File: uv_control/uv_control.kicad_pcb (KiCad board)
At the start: 2 copper layers, 20 parts, among them J1 Safety, J2 Fan, J3 12V Power, J4 Light Power, Q1 BSS138, Q2 BSS138, Q3 IRFS7730-7, U1 L7805, U2 MCP1415

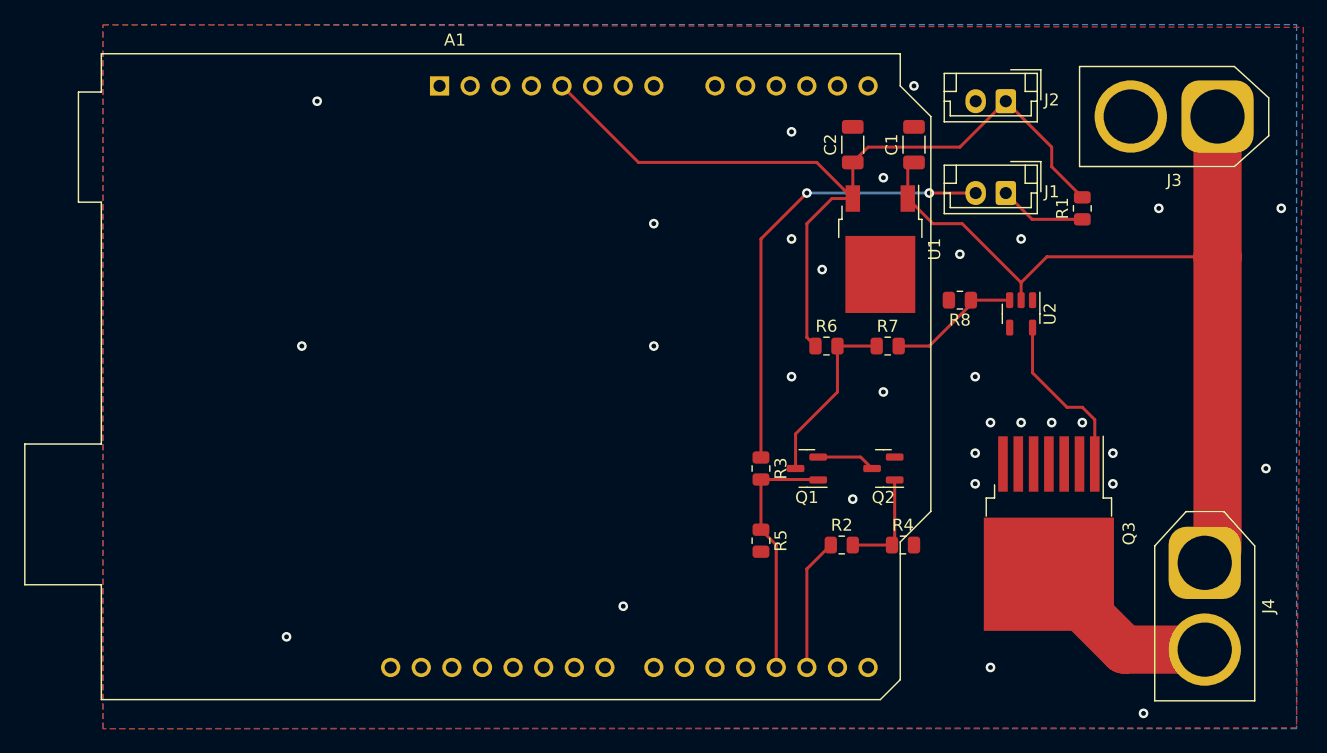
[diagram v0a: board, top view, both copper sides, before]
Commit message: Updating control board to include more pinouts
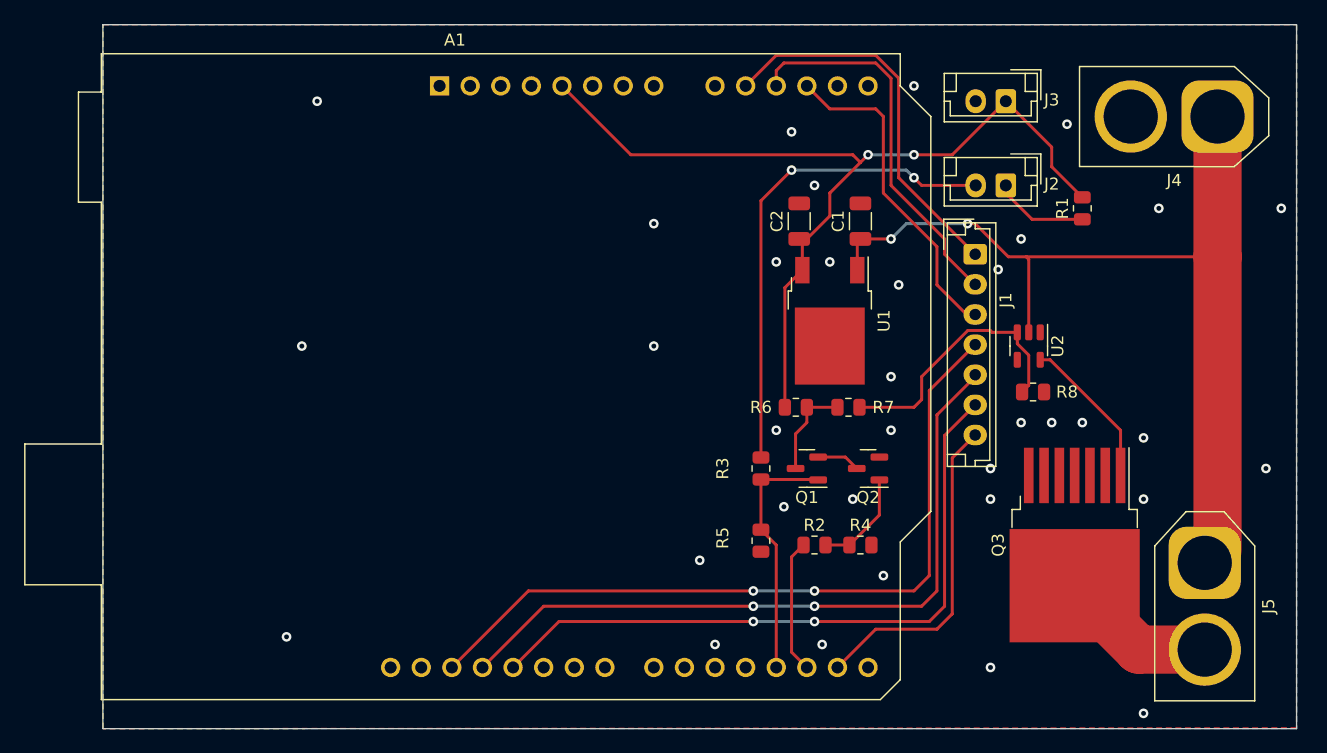
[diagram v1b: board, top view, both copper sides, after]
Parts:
- added J1: Keypad, Connector_JST:JST_EH_B7B-EH-A_1x07_P2.50mm_Vertical, F.Cu at (191.8, 85.1)
- moved R8 9.74 mm to (196.6, 96.5), turned to 0 degrees
- moved C2 7.75 mm to (177.2, 82.3)
- moved C1 7.75 mm to (182.2, 82.3)
- moved U1 7.27 mm to (179.7, 90.6)
- moved R7 6.03 mm to (181.3, 97.8)
- moved R6 5.68 mm to (176.9, 97.8)
- moved R4 3.53 mm to (182.2, 109.2)
- moved U2 2.75 mm to (196.2, 92.7)
- moved Q3 2.34 mm to (200.0, 109.2)
- moved R2 2.26 mm to (178.4, 109.2)
- moved Q2 1.27 mm to (182.9, 102.9)
- moved J2 0.64 mm to (194.3, 79.4)
- renumbered J1 to J2, J2 to J3, J3 to J4, J4 to J5
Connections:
- A1 pad 10: unconnected-(A1-Pad10) -> /Keypad_1
- A1 pad 11: unconnected-(A1-Pad11) -> /Keypad_2
- A1 pad 12: unconnected-(A1-Pad12) -> /Keypad_3
- A1 pad 16: unconnected-(A1-Pad16) -> Net-(A1-Pad16)
- A1 pad 26: unconnected-(A1-Pad26) -> Net-(A1-Pad26)
- A1 pad 27: unconnected-(A1-Pad27) -> Net-(A1-Pad27)
- A1 pad 28: unconnected-(A1-Pad28) -> Net-(A1-Pad28)
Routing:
- net Net-(A1-Pad28): track 0.00 -> 63.5 mm, vias 0 -> 2
- net Net-(A1-Pad27): track 0.00 -> 59.6 mm, vias 0 -> 2
- net Net-(A1-Pad26): track 0.00 -> 55.7 mm, vias 0 -> 2
- net /Keypad_1: track 0.00 -> 31.8 mm
- net /Keypad_2: track 0.00 -> 31.6 mm
- net /Keypad_3: track 0.00 -> 27.4 mm
- net Net-(A1-Pad16): track 0.00 -> 27.0 mm
- net Net-(R7-Pad2): track 11.0 -> 22.5 mm
- net Net-(Q1-Pad3): track 14.9 -> 8.01 mm
- net +12V: track 71.6 -> 77.8 mm, vias 0 -> 2
- net +5V: track 71.5 -> 75.7 mm, vias 0 -> 2
- net Net-(J2-Pad2): track 37.5 -> 40.7 mm
- net Net-(J5-Pad2): track 15.5 -> 13.0 mm
- net Net-(Q3-Pad1): track 14.2 -> 12.8 mm
- net Net-(Q1-Pad2): track 4.87 -> 3.60 mm
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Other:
- board outline added: 99.1 x 58.4 mm

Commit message: Updating PCB to change to 2 layer setup
Added LCD schematic, removing LCD shield design
Fixed XT60 polarity
Added Status LED and Safety LED
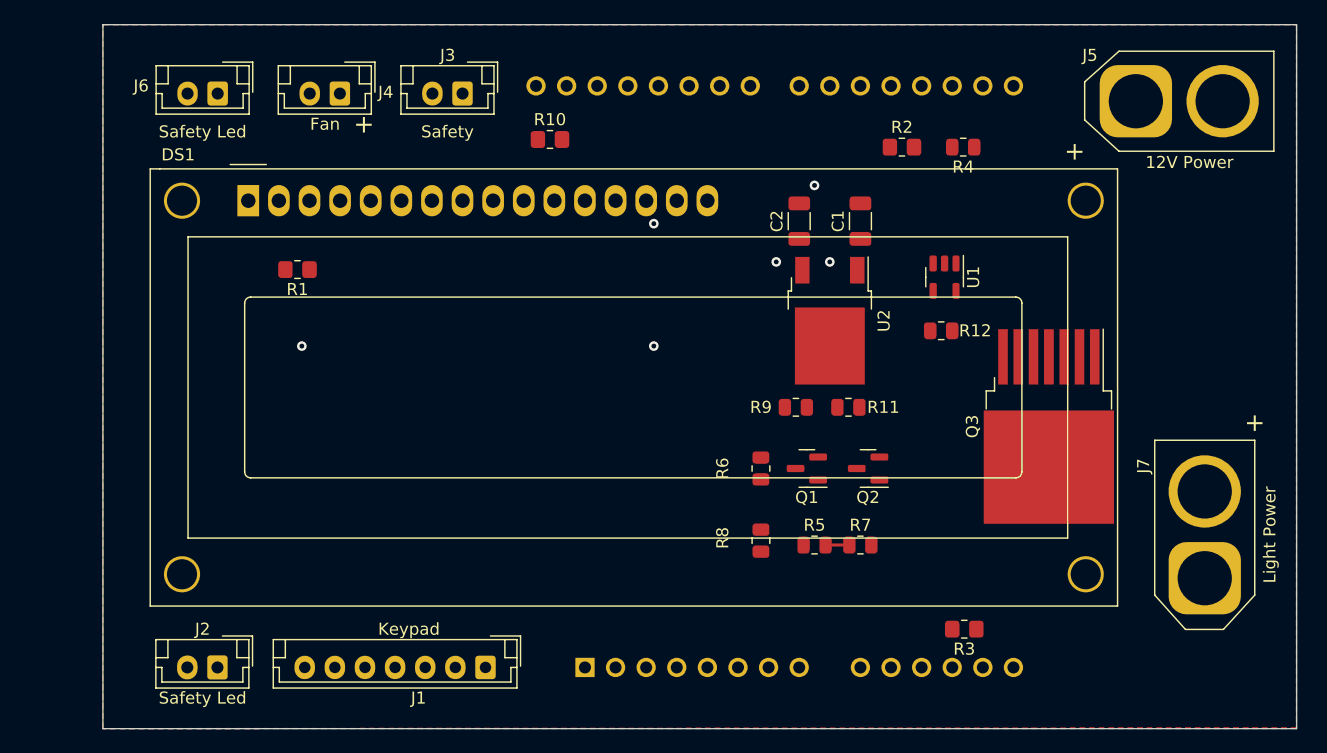
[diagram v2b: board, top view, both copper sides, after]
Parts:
- added DS1: WC1602A, Display:WC1602A, F.Cu at (131.4, 80.6)
- added J2: Safety Led, Connector_JST:JST_EH_B2B-EH-A_1x02_P2.50mm_Vertical, F.Cu at (128.9, 119.4)
- added J6: Safety Led, Connector_JST:JST_EH_B2B-EH-A_1x02_P2.50mm_Vertical, F.Cu at (128.9, 71.8)
- added R1: 10K, Resistor_SMD:R_0805_2012Metric_Pad1.20x1.40mm_HandSolder, F.Cu at (135.5, 86.4)
- added R10: 220, Resistor_SMD:R_0805_2012Metric_Pad1.20x1.40mm_HandSolder, F.Cu at (156.5, 75.6)
- added R2: 220, Resistor_SMD:R_0805_2012Metric_Pad1.20x1.40mm_HandSolder, F.Cu at (185.7, 76.2)
- added R3: 220, Resistor_SMD:R_0805_2012Metric_Pad1.20x1.40mm_HandSolder, F.Cu at (190.9, 116.2)
- A1: moved to B.Cu
- moved J4 55.3 mm to (139.0, 71.8)
- moved J1 53.2 mm to (151.1, 119.4), turned to 180 degrees
- moved A1 49.7 mm to (159.4, 119.4)
- moved J3 45.7 mm to (149.2, 71.8)
- moved R4 11.1 mm to (190.8, 76.2), turned to 180 degrees
- moved Q3 10.1 mm to (197.9, 99.4)
- moved R12 9.16 mm to (189.0, 91.4)
- moved U1 9.03 mm to (189.2, 87.0)
- moved J5 6.89 mm to (205.1, 72.4), turned to 0 degrees
- moved J7 1.27 mm to (210.8, 112.0), turned to 90 degrees
- renumbered J2 to J3, J3 to J4, J4 to J5, J5 to J7, R7 to R11, R8 to R12, R1 to R4, R2 to R5, R3 to R6, R4 to R7, R5 to R8, R6 to R9, U2 to U1, U1 to U2
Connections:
- net Net-(A1-Pad17) renamed /output_en
- A1 pad 13: unconnected-(A1-Pad13) -> /Keypad_4
- A1 pad 14: unconnected-(A1-Pad14) -> /safety_led
- A1 pad 16: Net-(A1-Pad16) -> unconnected-(A1-Pad16)
- A1 pad 19: unconnected-(A1-Pad19) -> /LCD_D4
- A1 pad 20: unconnected-(A1-Pad20) -> /LCD_D5
- A1 pad 21: unconnected-(A1-Pad21) -> /LCD_D6
- A1 pad 22: unconnected-(A1-Pad22) -> /LCD_D7
- A1 pad 23: unconnected-(A1-Pad23) -> /LCD_E
- A1 pad 24: unconnected-(A1-Pad24) -> /LCD_RS
- A1 pad 25: unconnected-(A1-Pad25) -> /status_led1
- J1 pad 7: Net-(A1-Pad16) -> /Keypad_4
- J5 pad 1: +12V -> GND
- J5 pad 2: GND -> +12V
- J7 pad 1: +12V -> Net-(Q3-Pad8)
- J7 pad 2: Net-(J5-Pad2) -> +12V
- Q3 pad 8: Net-(J5-Pad2) -> Net-(Q3-Pad8)
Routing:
- net +12V: track 77.8 -> 0.37 mm, vias 2 -> 0
- net +5V: track 75.7 -> 1.00 mm, vias 2 -> 0
- net Net-(A1-Pad28): track 63.5 -> 0.00 mm, vias 2 -> 0
- net Net-(A1-Pad27): track 59.6 -> 0.00 mm, vias 2 -> 0
- net Net-(A1-Pad26): track 55.7 -> 0.00 mm, vias 2 -> 0
- net Net-(J3-Pad2): track 40.7 -> 0.00 mm, vias 2 -> 0
- net /Keypad_1: track 31.8 -> 0.00 mm
- net /Keypad_2: track 31.6 -> 0.00 mm
- net /Keypad_3: track 27.4 -> 0.00 mm
- net Net-(A1-Pad16): track 27.0 -> 0.00 mm
- net Net-(R11-Pad2): track 22.5 -> 0.00 mm
- net /safety: track 20.9 -> 0.05 mm
- net Net-(J5-Pad2): track 13.0 -> 0.00 mm
- net Net-(Q3-Pad1): track 12.8 -> 0.00 mm
- net /output_en: track 11.1 -> 0.00 mm
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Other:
- board text added: "+"

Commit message: Reverting to V1 PCB in main branch
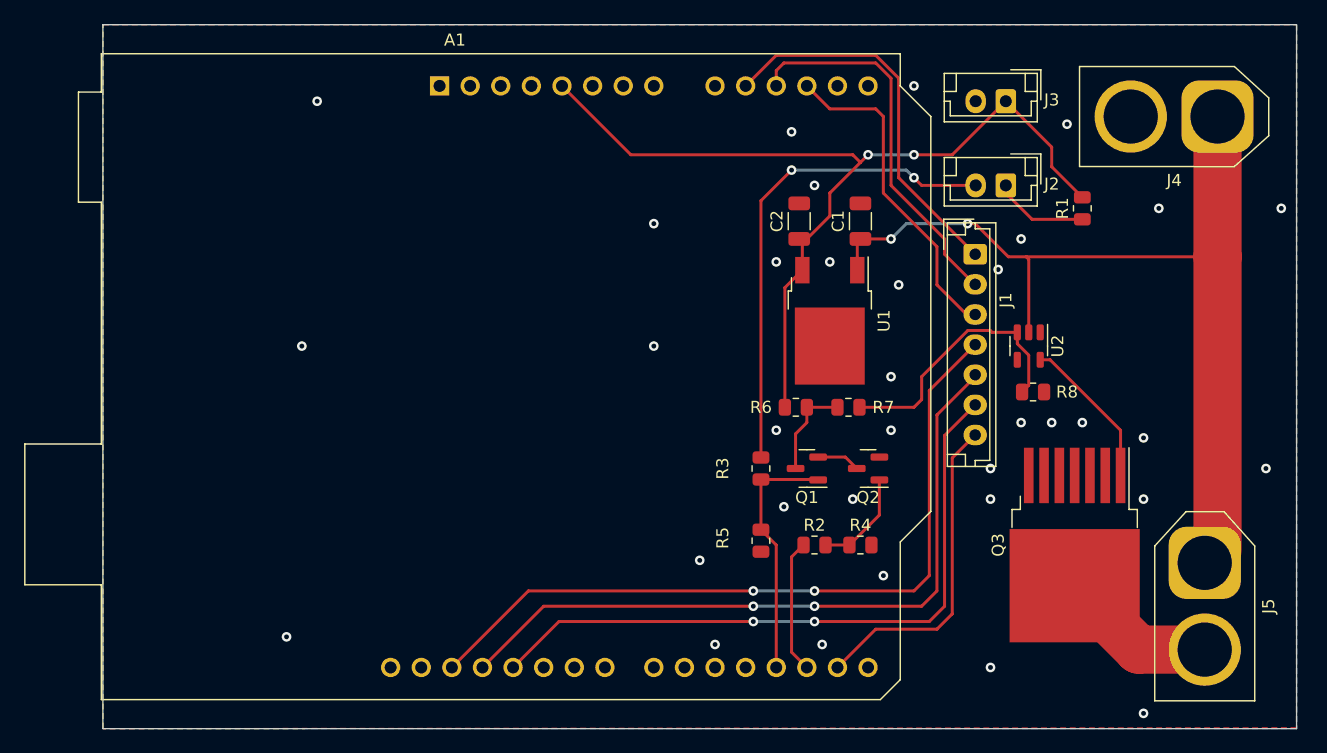
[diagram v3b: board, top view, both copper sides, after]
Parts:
- removed DS1: WC1602A, Display:WC1602A
- removed the J2 at (128.9, 119.4)
- removed J6: Safety Led, Connector_JST:JST_EH_B2B-EH-A_1x02_P2.50mm_Vertical
- removed the R1 at (135.5, 86.4)
- removed R10: 220, Resistor_SMD:R_0805_2012Metric_Pad1.20x1.40mm_HandSolder
- removed the R2 at (185.7, 76.2)
- removed the R3 at (190.9, 116.2)
- A1: moved to F.Cu
- moved J3 55.3 mm to (194.3, 72.4)
- moved J1 53.2 mm to (191.8, 85.1), turned to -90 degrees
- moved A1 49.7 mm to (147.3, 71.1)
- moved J2 45.7 mm to (194.3, 79.4)
- moved R1 11.1 mm to (200.7, 81.3), turned to 90 degrees
- moved Q3 10.1 mm to (200.0, 109.2)
- moved R8 9.16 mm to (196.6, 96.5)
- moved U2 9.03 mm to (196.2, 92.7)
- moved J4 6.89 mm to (211.9, 73.7), turned to 180 degrees
- moved J5 1.27 mm to (210.8, 110.7), turned to -90 degrees
- renumbered J3 to J2, J4 to J3, J5 to J4, J7 to J5, R4 to R1, R5 to R2, R6 to R3, R7 to R4, R8 to R5, R9 to R6, R11 to R7, R12 to R8, U2 to U1, U1 to U2
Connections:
- net /output_en renamed Net-(A1-Pad17)
- A1 pad 13: /Keypad_4 -> unconnected-(A1-Pad13)
- A1 pad 14: /safety_led -> unconnected-(A1-Pad14)
- A1 pad 16: unconnected-(A1-Pad16) -> Net-(A1-Pad16)
- A1 pad 19: /LCD_D4 -> unconnected-(A1-Pad19)
- A1 pad 20: /LCD_D5 -> unconnected-(A1-Pad20)
- A1 pad 21: /LCD_D6 -> unconnected-(A1-Pad21)
- A1 pad 22: /LCD_D7 -> unconnected-(A1-Pad22)
- A1 pad 23: /LCD_E -> unconnected-(A1-Pad23)
- A1 pad 24: /LCD_RS -> unconnected-(A1-Pad24)
- A1 pad 25: /status_led1 -> unconnected-(A1-Pad25)
- J1 pad 7: /Keypad_4 -> Net-(A1-Pad16)
- J4 pad 1: GND -> +12V
- J4 pad 2: +12V -> GND
- J5 pad 1: Net-(Q3-Pad8) -> +12V
- J5 pad 2: +12V -> Net-(J5-Pad2)
- Q3 pad 8: Net-(Q3-Pad8) -> Net-(J5-Pad2)
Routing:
- net +12V: track 0.37 -> 77.8 mm, vias 0 -> 2
- net +5V: track 1.00 -> 75.7 mm, vias 0 -> 2
- net Net-(A1-Pad28): track 0.00 -> 63.5 mm, vias 0 -> 2
- net Net-(A1-Pad27): track 0.00 -> 59.6 mm, vias 0 -> 2
- net Net-(A1-Pad26): track 0.00 -> 55.7 mm, vias 0 -> 2
- net Net-(J2-Pad2): track 0.00 -> 40.7 mm, vias 0 -> 2
- net /Keypad_1: track 0.00 -> 31.8 mm
- net /Keypad_2: track 0.00 -> 31.6 mm
- net /Keypad_3: track 0.00 -> 27.4 mm
- net Net-(A1-Pad16): track 0.00 -> 27.0 mm
- net Net-(R7-Pad2): track 0.00 -> 22.5 mm
- net /safety: track 0.05 -> 20.9 mm
- net Net-(J5-Pad2): track 0.00 -> 13.0 mm
- net Net-(Q3-Pad1): track 0.00 -> 12.8 mm
- net Net-(A1-Pad17): track 0.00 -> 11.1 mm
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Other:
- board text removed: "+"
